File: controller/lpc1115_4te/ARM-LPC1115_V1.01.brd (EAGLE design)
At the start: 66 x 57.9 mm, 100 parts, among them IC1 LPC1115, IC2 BD9G101, Q2 BCP52, Q3 BC856, Q4 12MHz, T1 BC547C

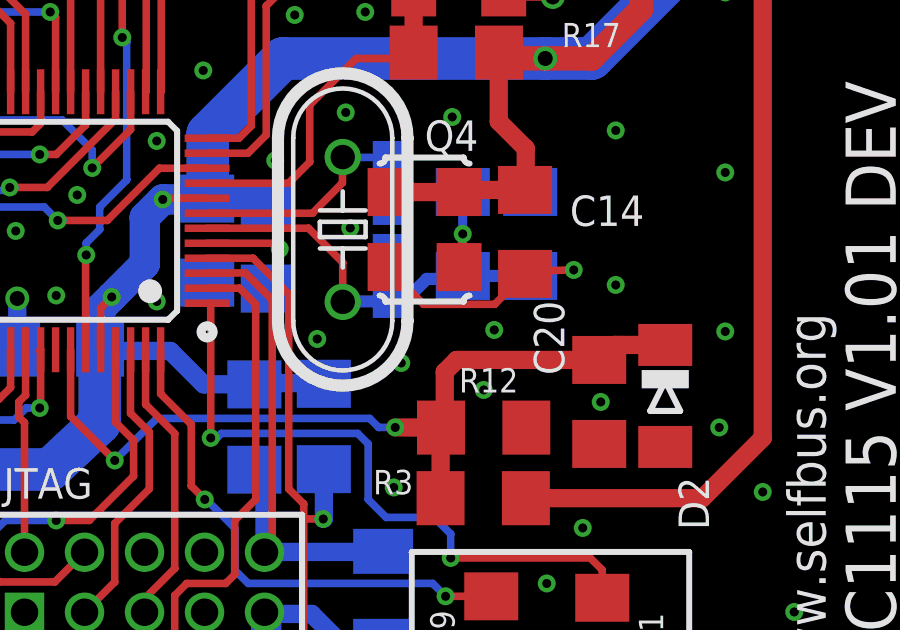
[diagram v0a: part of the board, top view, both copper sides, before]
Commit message: stoplackflaeche im via pin3 OSC zugefuegt
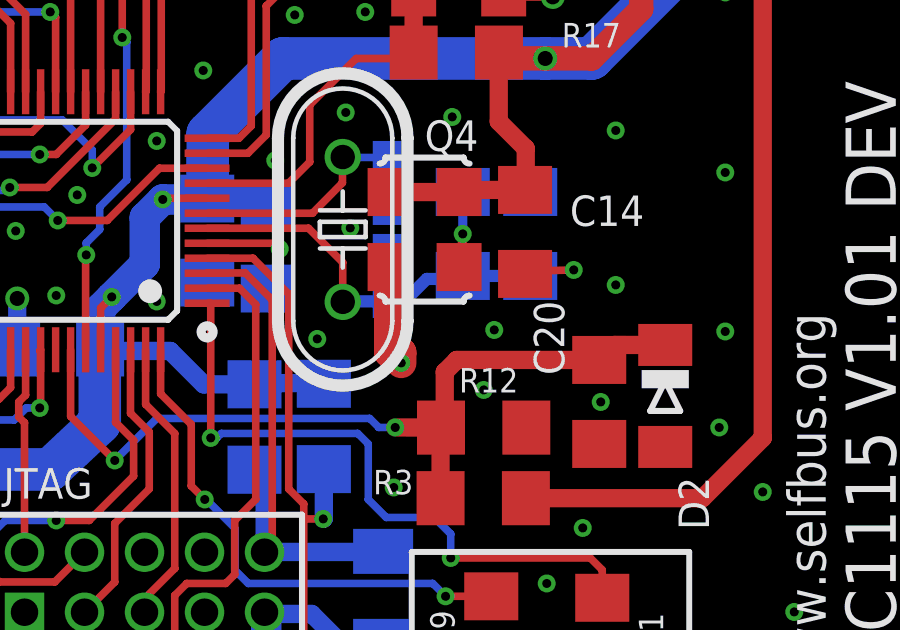
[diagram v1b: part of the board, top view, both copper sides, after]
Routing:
- net GND: track 274.6 -> 272.7 mm
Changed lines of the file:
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@@
 <circle x="48" y="36.2" radius="0.15" width="0" layer="30"/>
 <circle x="20.7" y="53.05" radius="0.15" width="0" layer="30"/>
+<circle x="51" y="23.15" radius="0.15" width="0" layer="30"/>
+<circle x="51" y="23.15" radius="0.15" width="0" layer="30"/>
 </plain>
 <attributes>
@@
 <wire x1="41.9662" y1="1.5794" x2="35.4638" y2="1.5794" width="1.27" layer="1"/>
 <contactref element="C11" pad="1"/>
-<wire x1="53.0778" y1="21.817275" x2="52.064775" y2="20.80425" width="0.254" layer="1"/>
-<wire x1="52.064775" y1="20.80425" x2="49.6965" y2="20.80425" width="0.254" layer="1"/>
-<wire x1="49.6965" y1="20.80425" x2="48.454125" y2="22.046625" width="0.254" layer="1"/>
 <wire x1="48.454125" y1="22.046625" x2="48.5782" y2="22.046625" width="0.254" layer="1"/>
 <wire x1="48.05" y1="22.4" x2="48.078075" y2="22.34025" width="0.254" layer="1"/>
@@
 <contactref element="C21" pad="2"/>
 <via x="47.25" y="23.35" extent="1-16" drill="0.3"/>
+<wire x1="48.454125" y1="22.046625" x2="48.55" y2="22.046625" width="1.016" layer="1"/>
+<wire x1="48.55" y1="22.046625" x2="48.55" y2="19.2" width="1.016" layer="1"/>
+<wire x1="48.55" y1="19.2" x2="48.95" y2="19.2" width="1.016" layer="1"/>
+<wire x1="48.95" y1="19.2" x2="48.95" y2="18.85" width="1.016" layer="1"/>
 </signal>
 <signal name="N$1">

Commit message: cap dividor value changed
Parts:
- C21: value 10p -> 220p
- C22: value 22p -> 100p
